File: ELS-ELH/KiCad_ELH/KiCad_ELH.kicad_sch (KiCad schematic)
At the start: 57 parts, among them J1 Pressure Transducer Screw Ter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, Q1 IRLZ44N, Q2 IRLZ44N, Q4 IRLZ44N, Q6 IRLZ44N

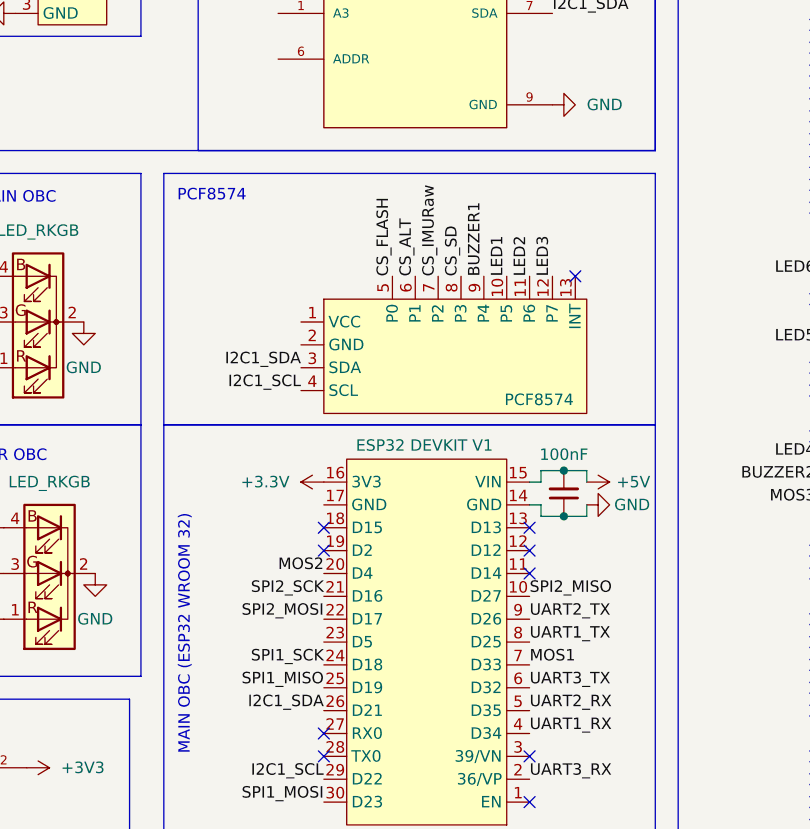
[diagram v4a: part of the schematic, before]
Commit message: Pin change
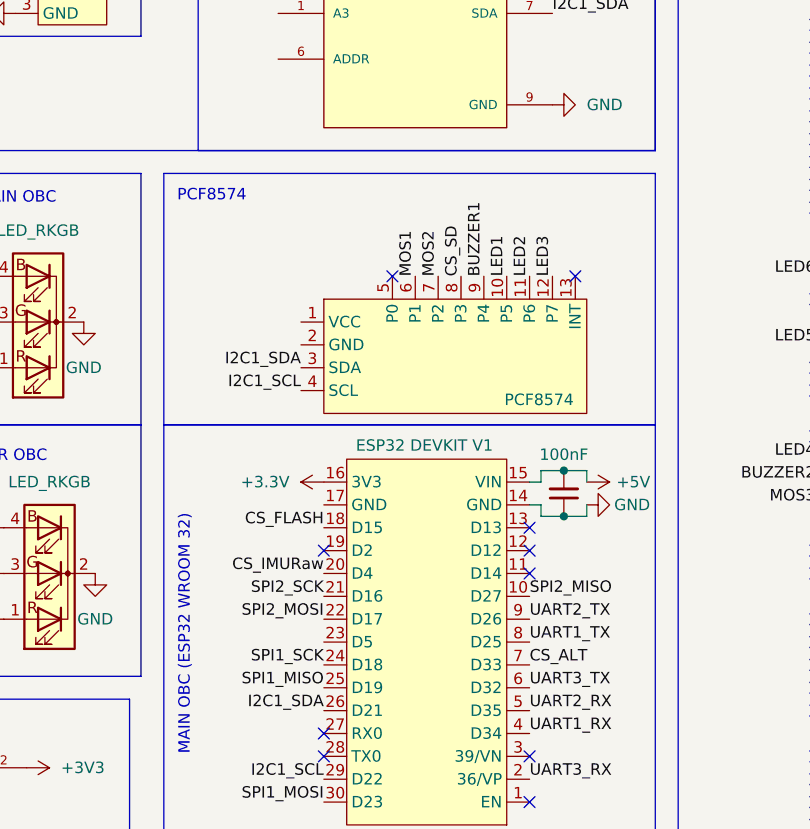
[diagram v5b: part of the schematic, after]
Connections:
- net CS_ALT: now also ESP1.7 (D33); no longer Adapter1.6 (P1)
- net CS_FLASH: now also ESP1.18 (D15); no longer Adapter1.5 (P0)
- net CS_IMURaw: now also ESP1.20 (D4); no longer Adapter1.7 (P2)
- net MOS1: now also Adapter1.6 (P1); no longer ESP1.7 (D33)
- net MOS2: now also Adapter1.7 (P2); no longer ESP1.20 (D4)
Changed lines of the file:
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@@
 	)
 	(no_connect
-		(at 167.64 118.11)
+		(at 175.26 90.17)
 	)
 	(no_connect
@@
 			(width 0)
 			(type default)
-		)
-	)
-	(label "CS_IMURaw"
-		(at 180.34 90.17 90)
-		(effects
-			(font
-				(size 1.27 1.27)
-			)
-			(justify left bottom)
 		)
 	)
@@
 		)
 	)
+	(label "CS_IMURaw"
+		(at 167.64 123.19 180)
+		(effects
+			(font
+				(size 1.27 1.27)
+			)
+			(justify right bottom)
+		)
+	)
 	(label "SPI1_MISO"
 		(at 31.75 177.8 180)
@@
 		)
 	)
+	(label "CS_FLASH"
+		(at 167.64 118.11 180)
+		(effects
+			(font
+				(size 1.27 1.27)
+			)
+			(justify right bottom)
+		)
+	)
 	(label "UART1_RX"
 		(at 262.89 120.65 0)
@@
 		)
 	)
-	(label "CS_FLASH"
-		(at 175.26 90.17 90)
-		(effects
-			(font
-				(size 1.27 1.27)
-			)
-			(justify left bottom)
-		)
-	)
-	(label "MOS1"
-		(at 190.5 133.35 0)
-		(effects
-			(font
-				(size 1.27 1.27)
-			)
-			(justify left bottom)
-		)
-	)
 	(label "UART2_RX"
 		(at 190.5 138.43 0)
@@
 		)
 	)
+	(label "CS_ALT"
+		(at 190.5 133.35 0)
+		(effects
+			(font
+				(size 1.27 1.27)
+			)
+			(justify left bottom)
+		)
+	)
 	(label "UART2_TX"
 		(at 264.16 38.1 0)
@@
 		)
 	)
+	(label "MOS2"
+		(at 180.34 90.17 90)
+		(effects
+			(font
+				(size 1.27 1.27)
+			)
+			(justify left bottom)
+		)
+	)
 	(label "SPI1_SCK"
 		(at 167.64 133.35 180)
@@
 		)
 	)
-	(label "CS_ALT"
-		(at 177.8 90.17 90)
-		(effects
-			(font
-				(size 1.27 1.27)
-			)
-			(justify left bottom)
-		)
-	)
 	(label "SPI1_MOSI"
 		(at 167.64 148.59 180)
@@
 		)
 	)
-	(label "MOS2"
-		(at 167.64 123.19 180)
-		(effects
-			(font
-				(size 1.27 1.27)
-			)
-			(justify right bottom)
-		)
-	)
 	(label "CS_SD"
 		(at 182.88 90.17 90)
@@
 		)
 	)
+	(label "MOS1"
+		(at 177.8 90.17 90)
+		(effects
+			(font
+				(size 1.27 1.27)
+			)
+			(justify left bottom)
+		)
+	)

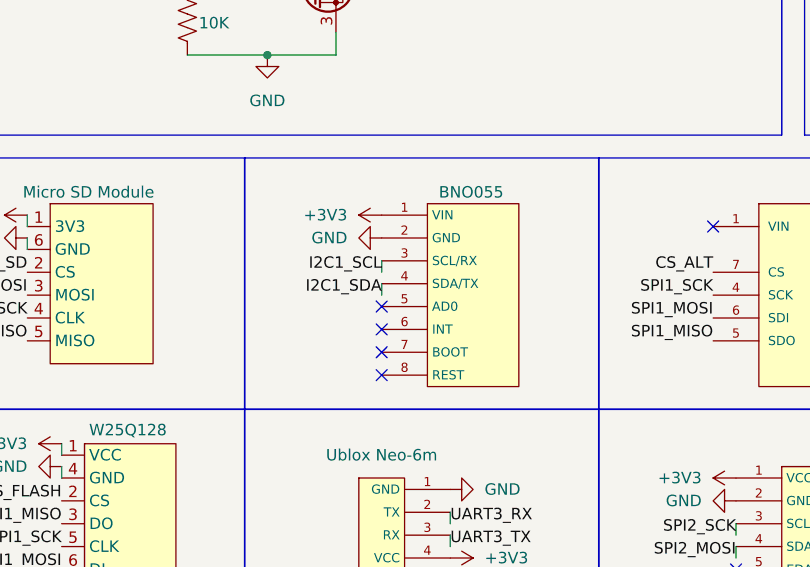
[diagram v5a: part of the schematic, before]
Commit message: Modification of the IMU Fused schematic
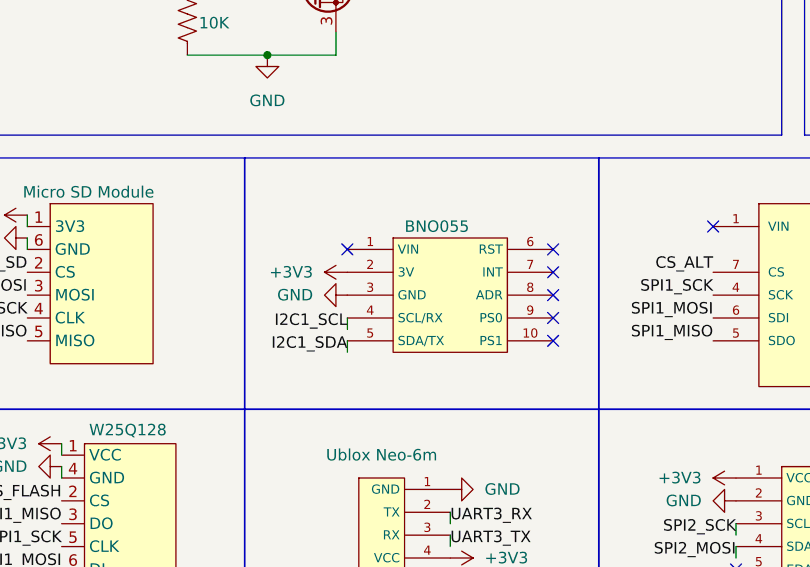
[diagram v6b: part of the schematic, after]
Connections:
- net +3V3: now also IMU3.2 (3V); no longer IMU3.1 (VIN)
- net GND: now also IMU3.3 (GND); no longer IMU3.2 (GND)
- net I2C1_SCL: now also IMU3.4 (SCL/RX); no longer IMU3.3 (SCL/RX)
- net I2C1_SDA: now also IMU3.5 (SDA/TX); no longer IMU3.4 (SDA/TX)
- no-connect marks 67 -> 69
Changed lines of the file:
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@@
 	)
 	(no_connect
+		(at 86.36 149.86)
+	)
+	(no_connect
+		(at 86.36 157.48)
+	)
+	(no_connect
 		(at 190.5 118.11)
 	)
@@
 	)
 	(no_connect
-		(at 67.31 156.21)
+		(at 86.36 147.32)
 	)
 	(no_connect
@@
 	)
 	(no_connect
-		(at 67.31 153.67)
-	)
-	(no_connect
 		(at 222.25 123.19)
 	)
 	(no_connect
-		(at 67.31 158.75)
+		(at 63.5 147.32)
 	)
 	(no_connect
@@
 	)
 	(no_connect
-		(at 67.31 161.29)
+		(at 86.36 152.4)
 	)
 	(no_connect
@@
 	)
 	(no_connect
+		(at 86.36 154.94)
+	)
+	(no_connect
 		(at 262.89 102.87)
 	)
@@
 	(wire
 		(pts
+			(xy 63.5 156.21) (xy 63.5 154.94)
+		)
+		(stroke
+			(width 0)
+			(type default)
+		)
+	)
+	(wire
+		(pts
 			(xy 60.96 30.48) (xy 67.31 30.48)
 		)
@@
 	(wire
 		(pts
-			(xy 67.31 149.86) (xy 67.31 148.59)
-		)
-		(stroke
-			(width 0)
-			(type default)
-		)
-	)
-	(wire
-		(pts
-			(xy 67.31 152.4) (xy 67.31 151.13)
-		)
-		(stroke
-			(width 0)
-			(type default)
-		)
-	)
-	(wire
-		(pts
 			(xy 165.1 29.21) (xy 167.64 29.21)
 		)
@@
 	(wire
 		(pts
+			(xy 63.5 158.75) (xy 63.5 157.48)
+		)
+		(stroke
+			(width 0)
+			(type default)
+		)
+	)
+	(wire
+		(pts
 			(xy 27.94 143.51) (xy 27.94 144.78)
 		)
@@
 		)
 	)
-	(label "I2C1_SCL"
-		(at 67.31 149.86 180)
-		(effects
-			(font
-				(size 1.27 1.27)
-			)
-			(justify right bottom)
-		)
-	)
 	(label "UART3_RX"
 		(at 190.5 146.05 0)
@@
 		)
 	)
+	(label "I2C1_SDA"
+		(at 63.5 158.75 180)
+		(effects
+			(font
+				(size 1.27 1.27)
+			)
+			(justify right bottom)
+		)
+	)
 	(label "MOS3"
 		(at 222.25 115.57 180)
@@
 		)
 	)
+	(label "I2C1_SCL"
+		(at 63.5 156.21 180)
+		(effects
+			(font
+				(size 1.27 1.27)
+			)
+			(justify right bottom)
+		)
+	)
 	(label "I2C1_SDA"
 		(at 167.64 138.43 180)
@@
 	)
 	(label "I2C1_SDA"
-		(at 67.31 152.4 180)
-		(effects
-			(font
-				(size 1.27 1.27)
-			)
-			(justify right bottom)
-		)
-	)
-	(label "I2C1_SDA"
 		(at 165.1 100.33 180)
 		(effects
@@
 	(symbol
 		(lib_id "power:+3V3")
-		(at 67.31 143.51 90)
+		(at 63.5 149.86 90)
 		(unit 1)
 		(exclude_from_sim no)
@@
 		(fields_autoplaced yes)
 		(property "Reference" "#PWR013"
-			(at 71.12 143.51 0)
+			(at 67.31 149.86 0)
 			(effects
 				(font
@@
 		)
 		(property "Value" "+3V3"
-			(at 63.5 143.5099 90)
+			(at 59.69 149.8599 90)
 			(effects
 				(font
@@
 		)
 		(property "Footprint" ""
-			(at 67.31 143.51 0)
+			(at 63.5 149.86 0)
 			(effects
 				(font
@@
 		)
 		(property "Datasheet" ""
-			(at 67.31 143.51 0)
+			(at 63.5 149.86 0)
 			(effects
 				(font
@@
 		)
 		(property "Description" "Power symbol creates a global label with name \"+3V3\""
-			(at 67.31 143.51 0)
+			(at 63.5 149.86 0)
 			(effects
 				(font
@@
 	(symbol
 		(lib_id "power:GND")
-		(at 67.31 146.05 270)
+		(at 63.5 152.4 270)
 		(unit 1)
 		(exclude_from_sim no)
@@
 		(fields_autoplaced yes)
 		(property "Reference" "#PWR021"
-			(at 60.96 146.05 0)
+			(at 57.15 152.4 0)
 			(effects
 				(font
@@
 		)
 		(property "Value" "GND"
-			(at 63.5 146.0499 90)
+			(at 59.69 152.3999 90)
 			(effects
 				(font
@@
 		)
 		(property "Footprint" ""
-			(at 67.31 146.05 0)
+			(at 63.5 152.4 0)
 			(effects
 				(font
@@
 		)
 		(property "Datasheet" ""
-			(at 67.31 146.05 0)
+			(at 63.5 152.4 0)
 			(effects
 				(font
@@
 		)
 		(property "Description" "Power symbol creates a global label with name \"GND\" , ground"
-			(at 67.31 146.05 0)
+			(at 63.5 152.4 0)
 			(effects
 				(font
@@
 	(symbol
 		(lib_id "ELH_Library:BNO055")
-		(at 76.2 142.24 0)
+		(at 72.39 146.05 0)
 		(unit 1)
 		(exclude_from_sim no)
@@
 		(dnp no)
 		(property "Reference" "IMU3"
-			(at 77.216 141.224 0)
+			(at 73.406 145.034 0)
 			(effects
 				(font
@@
 		)
 		(property "Value" "BNO055"
-			(at 73.66 140.97 0)
+			(at 69.85 144.78 0)
 			(effects
 				(font
@@
 		)
 		(property "Footprint" "ELH_Library:BNO055"
-			(at 76.2 142.24 0)
+			(at 72.39 146.05 0)
 			(effects
 				(font
@@
 		)
 		(property "Datasheet" "https://cdn-learn.adafruit.com/assets/assets/000/125/776/original/bst-bno055-ds000.pdf?1698865246"
-			(at 76.2 142.24 0)
+			(at 72.39 146.05 0)
 			(effects
 				(font
@@
 		)
 		(property "Description" "IMU Fused 9DoF"
-			(at 76.2 142.24 0)
+			(at 72.39 146.05 0)
 			(effects
 				(font
@@
 		(pin "8"
 		)
+		(pin "9"
+		)
+		(pin "10"
+		)
 		(instances

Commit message: Advances
Components almost ready, only 3 screw terminal footprints and component placement are needed
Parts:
- removed ADC1: ADS1115, ELH_Library:ADS1115, symbol ELH_Library:ADS1115
- removed Adapter1: PCF8574, ELH_Library:PCF8574, symbol ELH_Library:PCF8574
- removed BME2: BME280, ELH_Library:BME280, symbol ELH_Library:BME280
- removed BZ1: Buzzer, Buzzer_Beeper:Buzzer_12x9.5RM7.6, symbol Device:Buzzer
- removed Bornera7: COM Camera Screw Terminal, ELH_Library:Bornera 2P, symbol Connector:Screw_Terminal_01x02
- removed C10, C9: 47uF, symbol Device:C_Small
- removed C2, C4, C6, C8: 100nF, symbol Device:C_Small
- removed C3, C5, C7: 100uF, symbol Device:C_Small
- removed D10: LED_RKGB, LED_THT:LED_D5.0mm-4_RGB_Staggered_Pins, symbol Device:LED_RKGB
- removed ESP1: ESP32 DEVKIT V1, ELH_Library:ESP32 DEVKIT V1, symbol ELH_Library:ESP32 DEVKIT V1
- removed GPS1: Ublox Neo-6m, ELH_Library:Ublox Neo-6m, symbol ELH_Library:Ublox_Neo-6m
- removed IMU1: MPU9250, ELH_Library:MPU9250, symbol ELH_Library:MPU9250
- removed IMU3: BNO055, ELH_Library:BNO055, symbol ELH_Library:BNO055
- removed R12: 220, Resistor_THT:R_Axial_DIN0207_L6.3mm_D2.5mm_P7.62mm_Horizontal, symbol Device:R_US
- removed R4, R5, R7: 330, Resistor_THT:R_Axial_DIN0207_L6.3mm_D2.5mm_P7.62mm_Horizontal, symbol Device:R_US
- removed Regulator2: MP1584, symbol ELH_Library:MP1584
- removed SD_Adapter1: Micro SD Module, ELH_Library:MicroSD Module, symbol ELH_Library:Micro SD Module
- removed W25QXX1: W25Q128, symbol ELH_Library:W25Q128
- added C10, C9: 47uF, Capacitor_THT:CP_Radial_D6.3mm_P2.50mm, symbol Device:C_Polarized_Small
- added C3: 10uF, Capacitor_THT:CP_Radial_D5.0mm_P2.50mm, symbol Device:C_Polarized_Small
- added Driver_DC2: TB6612FNG, ELH_Library:TB6612FNG, symbol ELH_Library:TB6612FNG
- added J11: RW2 Screw Terminal, symbol Connector:Screw_Terminal_01x04
- added J3: MOSFETS MAIN, ELH_Library:2Pin Header, symbol Connector:Conn_01x02_Pin
- added J5: COM CTR-MAIN, ELH_Library:2Pin Header, symbol Connector:Conn_01x02_Pin
- added J6: Sensors, ELH_Library:2Pin Header, symbol Connector:Conn_01x02_Pin
- added J8: RW1 Screw Terminal, symbol Connector:Screw_Terminal_01x04
- added J9: Pressure Transducer, ELH_Library:3Pin Header, symbol Connector:Conn_01x03_Pin
- added Regulator3: MP1584, ELH_Library:MP1584, symbol ELH_Library:MP1584
- C1: footprint (none) -> Capacitor_THT:C_Disc_D5.0mm_W2.5mm_P5.00mm
- Regulator1: footprint (none) -> ELH_Library:LM1117T
- Regulator4: footprint (none) -> ELH_Library:MP1584
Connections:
- net +12V: now also Regulator4.4 (OUTPUT+), C10.1, C9.1, Driver_DC2.1 (VM), J11.3 (Pin_3), J8.2 (Pin_2), Regulator3.2 (IN+); no longer Regulator4. (OUTPUT+)
- net +3V3: now also J6.1 (Pin_1)
- net +5V: now also C3.1, J9.1 (Pin_1)
- net GND: now also Regulator4.3 (OUTPUT-), C3.2, Driver_DC2.3 (GND), Driver_DC2.8 (GND), Driver_DC2.9 (GND), J11.4 (Pin_4), J6.2 (Pin_2), J8.1 (Pin_1), J9.2 (Pin_2), Regulator3.1 (IN-); no longer BZ2.2 (-), D3.2 (K), Regulator4. (OUTPUT+)
- net at Bornera4.1 (Pin_1), D1.2 (A), Q1.2 (D): now also C10.2
- net at Bornera5.1 (Pin_1), D9.2 (A), Q6.2 (D): now also C9.2
- net at Bornera3.1 (Pin_1): now also Regulator3.3 (OUTPUT-); no longer Regulator4. (OUTPUT+)
- net at Bornera3.2 (Pin_2): now also Regulator3.4 (OUTPUT+); no longer Regulator4. (OUTPUT+)
- net at Bornera6.1 (Pin_1): now also Regulator4.2 (IN+)
- net at Bornera6.2 (Pin_2): now also Regulator4.1 (IN-)
- net PWMA: now reaches Teensy3.14 (A0)
- net PWMA: now also Driver_DC2.16 (PWMA)
- net AIN1: now reaches Teensy3.15 (A1)
- net AIN1: now also Driver_DC2.14 (AI1)
- net AIN2: now reaches Teensy3.16 (A2)
- net AIN2: now also Driver_DC2.15 (AI2)
- net PWMB: now reaches Teensy3.17 (A3)
- net PWMB: now also Driver_DC2.10 (PWMB)
- net BIN1: now reaches Teensy3.18 (A4)
- net BIN1: now also Driver_DC2.12 (BI1)
- net BIN2: now reaches Teensy3.19 (A5)
- net BIN2: now also Driver_DC2.11 (BI2)
- net STBY: now reaches Teensy3.20 (A6)
- net STBY: now also Driver_DC2.13 (STBY)
- net 3.3V renamed +3.3VA
- net +3.3VA: now also Driver_DC2.2 (VCC)
- net MOS1 renamed MOS1_1
- net MOS1_1: now also J3.1 (Pin_1)
- net MOS2 renamed MOS2_1
- net MOS2_1: now also J3.2 (Pin_2)
- net PT_ADC renamed PT_ADC1
- net PT_ADC1: now also J9.3 (Pin_3)
- net UART1_RX renamed UART1_RX_1
- net UART1_RX_1: now also J5.1 (Pin_1)
- net UART1_TX renamed UART1_TX_1
- net UART1_TX_1: now also J5.2 (Pin_2)
- new net: Driver_DC2.4 (A01), J8.3 (Pin_3)
- new net: Driver_DC2.5 (A02), J8.4 (Pin_4)
- new net: Driver_DC2.6 (B02), J11.2 (Pin_2)
- new net: Driver_DC2.7 (B01), J11.1 (Pin_1)
- new net GND1: BZ2.2 (-), D3.2 (K)
- no-connect marks 69 -> 41
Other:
- added sheet sensors (sensors.kicad_sch)
- note added: "Reaction Wheels"
- note added: "Screw Terminals"
- note removed: "BUZZER MAIN OBC"
- note removed: "LEDs MAIN OBC"
- note removed: "MAIN OBC (ESP32 WROOM 32)"
- note removed: "PCF8574"

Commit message: Components preliminar distribution
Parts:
- removed Bornera1: Sensor Power Supply Screw Terminal, ELH_Library:Bornera 2P, symbol Connector:Screw_Terminal_01x02
- removed J11: RW2 Screw Terminal, symbol Connector:Screw_Terminal_01x04
- removed J3: MOSFETS MAIN, ELH_Library:2Pin Header, symbol Connector:Conn_01x02_Pin
- removed J5: COM CTR-MAIN, ELH_Library:2Pin Header, symbol Connector:Conn_01x02_Pin
- removed J6: Sensors, ELH_Library:2Pin Header, symbol Connector:Conn_01x02_Pin
- removed J9: Pressure Transducer, ELH_Library:3Pin Header, symbol Connector:Conn_01x03_Pin
- added Bornera2: Camera Screw Terminal, ELH_Library:Bornera 2P, symbol Connector:Screw_Terminal_01x02_1
- added J2: Conn_01x09_Pin, Connector_Hirose:Hirose_DF13-09P-1.25DSA_1x09_P1.25mm_Vertical, symbol Connector:Conn_01x09_Pin
- Bornera3: value Camera Screw Terminal -> Actuator Power Supply Screw Terminal
- Bornera6: value Actuator Power Supply Screw Terminal -> Sensor Power Supply Screw Terminal
- J1: footprint (none) -> TerminalBlock:TerminalBlock_MaiXu_MX126-5.0-03P_1x03_P5.00mm
- J8: footprint (none) -> TerminalBlock:TerminalBlock_MaiXu_MX126-5.0-04P_1x04_P5.00mm
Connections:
- net +3V3: now also J2.5 (Pin_5)
- net +5V: now also J2.7 (Pin_7)
- net GND: now also J2.6 (Pin_6), J2.8 (Pin_8)
- net MOS1_1: now also J2.1 (Pin_1)
- net MOS2_1: now also J2.2 (Pin_2)
- net PT_ADC1: now also J2.9 (Pin_9)
- net UART1_RX_1: now also J2.3 (Pin_3)
- net UART1_TX_1: now also J2.4 (Pin_4)
- net at BOOST1.1 (IN+): now also Bornera6.1 (Pin_2)
- net at BOOST1.2 (IN-): now also Bornera6.2 (Pin_1)
- net at Regulator4.1 (IN-): now also Bornera3.1 (Pin_2); no longer Bornera6.2 (Pin_2)
- net at Regulator4.2 (IN+): now also Bornera3.2 (Pin_1); no longer Bornera6.1 (Pin_1)
- net at Regulator3.3 (OUTPUT-): now also Bornera2.2 (Pin_1); no longer Bornera3.1 (Pin_1)
- net at Regulator3.4 (OUTPUT+): now also Bornera2.1 (Pin_2); no longer Bornera3.2 (Pin_2)
- no-connect marks 41 -> 44
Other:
- note added: "Headers"
- note removed: "Screw Terminals"
